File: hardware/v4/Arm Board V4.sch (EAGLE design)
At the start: 43 parts, among them U1 SN74LS241DW, U2 XBEE-1B3, U3 LSM9DS0

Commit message: Nothing much
Nothing much
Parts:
- removed H1, H2, H3, H4: (no value), Lib_TH:H_MNTHOLE_#4
- removed JP4: (no value), SparkFun-Connectors:M04SCREW
- added JP1: (no value), SparkFun-Connectors:M03SCREW
- added S1, S2, S3, S4: STANDOFF_ELECTRICAL, SparkFun-Electromechanical:STANDOFF_ELECTRICAL
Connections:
- net +12V: now also JP1.3; no longer JP4.3
- net +5V: now also U$3.4, U$3.5; no longer JP4.4
- net GND: now also JP1.1, S1.P$1, S2.P$1, S3.P$1, S4.P$1; no longer H1.1, H2.1, H3.1, H4.1, JP4.1
- net VIN: now also JP1.2; no longer JP4.2
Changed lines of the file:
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@@
 <part name="R11" library="SparkFun-Passives" deviceset="RESISTOR" device="1206" value="120 Ohm"/>
 <part name="C12" library="SparkFun-Capacitors" deviceset="CAP" device="1206" value=".1uF"/>
-<part name="H1" library="Lib_TH" deviceset="H_MNTHOLE" device="_#4"/>
-<part name="H2" library="Lib_TH" deviceset="H_MNTHOLE" device="_#4"/>
-<part name="H3" library="Lib_TH" deviceset="H_MNTHOLE" device="_#4"/>
-<part name="H4" library="Lib_TH" deviceset="H_MNTHOLE" device="_#4"/>
-<part name="GND11" library="SparkFun-Aesthetics" deviceset="GND" device=""/>
-<part name="GND12" library="SparkFun-Aesthetics" deviceset="GND" device=""/>
-<part name="GND13" library="SparkFun-Aesthetics" deviceset="GND" device=""/>
-<part name="GND14" library="SparkFun-Aesthetics" deviceset="GND" device=""/>
 <part name="R12" library="SparkFun-Passives" deviceset="RESISTOR" device="1206" value="1k"/>
 <part name="LED1" library="SparkFun-LED" deviceset="LED-RED" device="0603" value="RED"/>
@@
 <part name="LED5" library="SparkFun-LED" deviceset="LED-RED" device="0603" value="RED"/>
 <part name="GND30" library="SparkFun" deviceset="GND" device=""/>
-<part name="JP4" library="SparkFun-Connectors" deviceset="M04" device="SCREW"/>
-<part name="GND3" library="SparkFun-Aesthetics" deviceset="GND" device=""/>
+<part name="S1" library="SparkFun-Electromechanical" deviceset="STANDOFF_ELECTRICAL" device=""/>
+<part name="S2" library="SparkFun-Electromechanical" deviceset="STANDOFF_ELECTRICAL" device=""/>
+<part name="S3" library="SparkFun-Electromechanical" deviceset="STANDOFF_ELECTRICAL" device=""/>
+<part name="S4" library="SparkFun-Electromechanical" deviceset="STANDOFF_ELECTRICAL" device=""/>
+<part name="GND11" library="SparkFun-Aesthetics" deviceset="GND" device=""/>
+<part name="JP1" library="SparkFun-Connectors" deviceset="M03" device="SCREW"/>
+<part name="GND12" library="SparkFun-Aesthetics" deviceset="GND" device=""/>
 </parts>
 <sheets>
@@
 </plain>
 <instances>
-<instance part="H1" gate="G$1" x="25.4" y="38.1"/>
-<instance part="H2" gate="G$1" x="35.56" y="38.1"/>
-<instance part="H3" gate="G$1" x="45.72" y="38.1"/>
-<instance part="H4" gate="G$1" x="55.88" y="38.1"/>
-<instance part="GND11" gate="1" x="25.4" y="30.48"/>
-<instance part="GND12" gate="1" x="35.56" y="30.48"/>
-<instance part="GND13" gate="1" x="45.72" y="30.48"/>
-<instance part="GND14" gate="1" x="55.88" y="30.48"/>
 <instance part="JP7" gate="G$1" x="190.5" y="50.8" rot="R270"/>
 <instance part="JP8" gate="G$1" x="203.2" y="50.8" rot="R270"/>
@@
 <instance part="LED5" gate="G$1" x="15.24" y="-25.4"/>
 <instance part="GND30" gate="1" x="15.24" y="-35.56"/>
-<instance part="JP4" gate="G$1" x="129.54" y="10.16" rot="R270"/>
-<instance part="GND3" gate="1" x="127" y="2.54"/>
+<instance part="S1" gate="G$1" x="25.4" y="58.42" rot="R270"/>
+<instance part="S2" gate="G$1" x="38.1" y="58.42" rot="R270"/>
+<instance part="S3" gate="G$1" x="50.8" y="58.42" rot="R270"/>
+<instance part="S4" gate="G$1" x="63.5" y="58.42" rot="R270"/>
+<instance part="GND11" gate="1" x="43.18" y="45.72"/>
+<instance part="JP1" gate="G$1" x="152.4" y="12.7" rot="R270"/>
+<instance part="GND12" gate="1" x="149.86" y="2.54"/>
 </instances>
 <busses>
@@
 <net name="GND" class="0">
 <segment>
-<pinref part="H1" gate="G$1" pin="1"/>
-<pinref part="GND11" gate="1" pin="GND"/>
-<wire x1="25.4" y1="33.02" x2="25.4" y2="38.1" width="0.1524" layer="91"/>
-</segment>
-<segment>
-<pinref part="H2" gate="G$1" pin="1"/>
-<pinref part="GND12" gate="1" pin="GND"/>
-<wire x1="35.56" y1="33.02" x2="35.56" y2="38.1" width="0.1524" layer="91"/>
-</segment>
-<segment>
-<pinref part="H3" gate="G$1" pin="1"/>
-<pinref part="GND13" gate="1" pin="GND"/>
-<wire x1="45.72" y1="33.02" x2="45.72" y2="38.1" width="0.1524" layer="91"/>
-</segment>
-<segment>
-<pinref part="H4" gate="G$1" pin="1"/>
-<pinref part="GND14" gate="1" pin="GND"/>
-<wire x1="55.88" y1="33.02" x2="55.88" y2="38.1" width="0.1524" layer="91"/>
-</segment>
-<segment>
 <pinref part="JP9" gate="G$1" pin="1"/>
 <pinref part="GND1" gate="1" pin="GND"/>
@@
 </segment>
 <segment>
-<pinref part="JP4" gate="G$1" pin="1"/>
-<pinref part="GND3" gate="1" pin="GND"/>
+<pinref part="S1" gate="G$1" pin="P$1"/>
+<wire x1="25.4" y1="50.8" x2="25.4" y2="48.26" width="0.1524" layer="91"/>
+<pinref part="GND11" gate="1" pin="GND"/>
+<wire x1="25.4" y1="48.26" x2="38.1" y2="48.26" width="0.1524" layer="91"/>
+<pinref part="S2" gate="G$1" pin="P$1"/>
+<wire x1="43.18" y1="48.26" x2="38.1" y2="48.26" width="0.1524" layer="91"/>
+<wire x1="38.1" y1="50.8" x2="38.1" y2="48.26" width="0.1524" layer="91"/>
+<pinref part="S4" gate="G$1" pin="P$1"/>
+<wire x1="63.5" y1="50.8" x2="63.5" y2="48.26" width="0.1524" layer="91"/>
+<wire x1="63.5" y1="48.26" x2="50.8" y2="48.26" width="0.1524" layer="91"/>
+<pinref part="S3" gate="G$1" pin="P$1"/>
+<wire x1="50.8" y1="48.26" x2="43.18" y2="48.26" width="0.1524" layer="91"/>
+<wire x1="50.8" y1="50.8" x2="50.8" y2="48.26" width="0.1524" layer="91"/>
+<junction x="38.1" y="48.26"/>
+<junction x="50.8" y="48.26"/>
+<junction x="43.18" y="48.26"/>
+<junction x="25.4" y="48.26"/>
+<junction x="63.5" y="48.26"/>
+</segment>
+<segment>
+<pinref part="JP1" gate="G$1" pin="1"/>
+<pinref part="GND12" gate="1" pin="GND"/>
 </segment>
 </net>
@@
 </segment>
 <segment>
-<pinref part="JP4" gate="G$1" pin="3"/>
-<wire x1="132.08" y1="5.08" x2="132.08" y2="-10.16" width="0.1524" layer="91"/>
-<label x="132.08" y="-5.08" size="1.778" layer="95" rot="R270"/>
+<wire x1="154.94" y1="5.08" x2="154.94" y2="-5.08" width="0.1524" layer="91"/>
+<pinref part="JP1" gate="G$1" pin="3"/>
 </segment>
 </net>
@@
 <wire x1="190.5" y1="43.18" x2="190.5" y2="38.1" width="0.1524" layer="91"/>
 <label x="190.5" y="38.1" size="1.778" layer="95" rot="R180"/>
-</segment>
-<segment>
-<pinref part="JP4" gate="G$1" pin="4"/>
-<wire x1="134.62" y1="5.08" x2="134.62" y2="-17.78" width="0.1524" layer="91"/>
-<label x="134.62" y="-15.24" size="1.778" layer="95" rot="R270"/>
 </segment>
 </net>
@@
 </segment>
 <segment>
-<pinref part="JP4" gate="G$1" pin="2"/>
-<wire x1="129.54" y1="5.08" x2="129.54" y2="-2.54" width="0.1524" layer="91"/>
-<label x="129.54" y="-2.54" size="1.778" layer="95" rot="R270"/>
+<wire x1="152.4" y1="5.08" x2="152.4" y2="-2.54" width="0.1524" layer="91"/>
+<pinref part="JP1" gate="G$1" pin="2"/>
 </segment>
 </net>
@@
 <pinref part="U$4" gate="G$1" pin="VCC"/>
 </segment>
-</net>
+<segment>
+<pinref part="U$3" gate="G$1" pin="4"/>
+<wire x1="132.08" y1="15.24" x2="129.54" y2="15.24" width="0.1524" layer="91"/>
+<wire x1="129.54" y1="15.24" x2="129.54" y2="12.7" width="0.1524" layer="91"/>
+<pinref part="U$3" gate="G$1" pin="5"/>
+<wire x1="129.54" y1="12.7" x2="132.08" y2="12.7" width="0.1524" layer="91"/>
+</segment>
+</net>

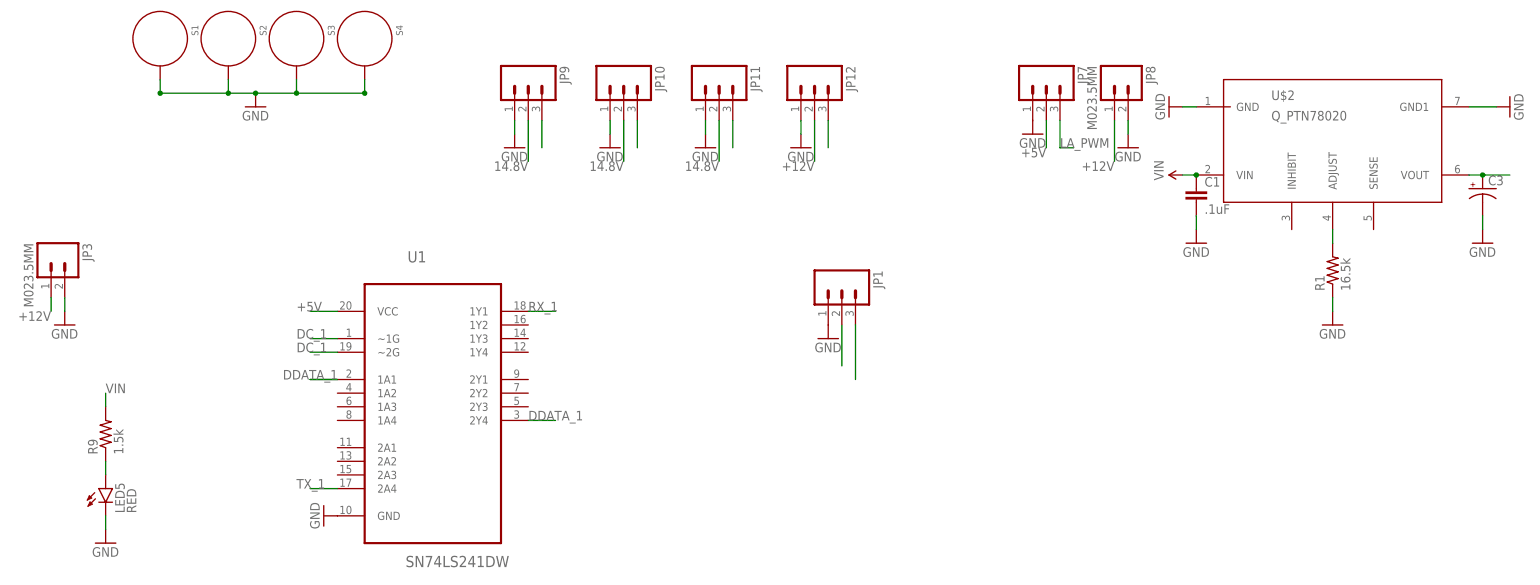
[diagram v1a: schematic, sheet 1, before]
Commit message: Implemented PoRN and Switched Power Connectors
Implemented PoRN(PoRC) and switched to 3.5mm screw terminals
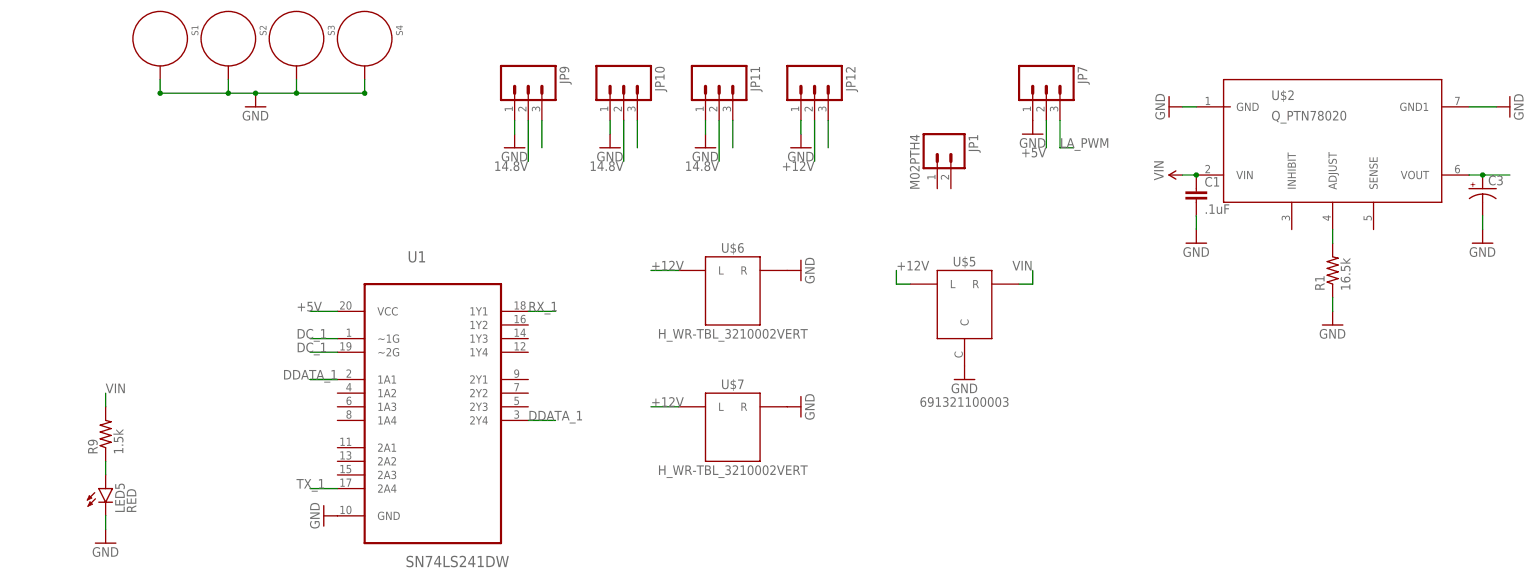
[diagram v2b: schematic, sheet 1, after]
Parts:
- removed JP3, JP8: M023.5MM, SparkFun-Connectors:M023.5MM
- added U$5: 691321100003, MRDT-2015-PowerBoard:691321100003
- added U$6, U$7: H_WR-TBL_3210002VERT, MRDT-2015-PowerBoard:H_WR-TBL_3210002VERT
- JP1: value (none) -> M02PTH4; device SparkFun-Connectors:M03SCREW -> SparkFun-Connectors:M02PTH4
- JP10, JP11, JP12, JP7, JP9: device SparkFun-Connectors:M03POLAR -> SparkFun-Connectors:M03PTH
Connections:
- net +12V: now also U$5.L, U$6.L, U$7.L; no longer JP1.3, JP3.1, JP8.1
- net GND: now also U$5.C, U$6.R, U$7.R; no longer JP1.1, JP3.2, JP8.2
- net VIN: now also U$5.R; no longer JP1.2
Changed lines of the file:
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@@
 <part name="R14" library="SparkFun-Passives" deviceset="RESISTOR" device="1206" value="1k"/>
 <part name="U2" library="SparkFun" deviceset="XBEE-1" device="B3"/>
-<part name="JP7" library="SparkFun-Connectors" deviceset="M03" device="POLAR"/>
-<part name="JP8" library="SparkFun-Connectors" deviceset="M02" device="3.5MM" value="M023.5MM"/>
-<part name="JP9" library="SparkFun-Connectors" deviceset="M03" device="POLAR"/>
-<part name="JP10" library="SparkFun-Connectors" deviceset="M03" device="POLAR"/>
-<part name="JP11" library="SparkFun-Connectors" deviceset="M03" device="POLAR"/>
-<part name="JP12" library="SparkFun-Connectors" deviceset="M03" device="POLAR"/>
+<part name="JP7" library="SparkFun-Connectors" deviceset="M03" device="PTH"/>
+<part name="JP9" library="SparkFun-Connectors" deviceset="M03" device="PTH"/>
+<part name="JP10" library="SparkFun-Connectors" deviceset="M03" device="PTH"/>
+<part name="JP11" library="SparkFun-Connectors" deviceset="M03" device="PTH"/>
+<part name="JP12" library="SparkFun-Connectors" deviceset="M03" device="PTH"/>
 <part name="GND1" library="SparkFun-Aesthetics" deviceset="GND" device=""/>
 <part name="GND2" library="SparkFun-Aesthetics" deviceset="GND" device=""/>
 <part name="GND4" library="SparkFun-Aesthetics" deviceset="GND" device=""/>
 <part name="GND5" library="SparkFun-Aesthetics" deviceset="GND" device=""/>
-<part name="GND9" library="SparkFun-Aesthetics" deviceset="GND" device=""/>
 <part name="GND10" library="SparkFun-Aesthetics" deviceset="GND" device=""/>
 <part name="U$2" library="MRDT-2014-All" deviceset="Q_PTN78020" device=""/>
@@
 <part name="C3" library="SparkFun-Passives" deviceset="CAP_POL" device="C"/>
 <part name="U$4" library="MAX3077" deviceset="MAX3077" device=""/>
-<part name="JP3" library="SparkFun-Connectors" deviceset="M02" device="3.5MM" value="M023.5MM"/>
-<part name="GND6" library="SparkFun-Aesthetics" deviceset="GND" device=""/>
 <part name="U3" library="SparkFun-DigitalIC" deviceset="LSM9DS0" device=""/>
 <part name="C5" library="SparkFun-Capacitors" deviceset="CAP" device="1206" value=".22uF"/>
@@
 <part name="S4" library="SparkFun-Electromechanical" deviceset="STANDOFF_ELECTRICAL" device=""/>
 <part name="GND11" library="SparkFun-Aesthetics" deviceset="GND" device=""/>
-<part name="JP1" library="SparkFun-Connectors" deviceset="M03" device="SCREW"/>
-<part name="GND12" library="SparkFun-Aesthetics" deviceset="GND" device=""/>
+<part name="U$5" library="MRDT-2015-PowerBoard" deviceset="691321100003" device=""/>
+<part name="GND3" library="SparkFun-Aesthetics" deviceset="GND" device=""/>
+<part name="U$6" library="MRDT-2015-PowerBoard" deviceset="H_WR-TBL_32*1*0002" device="VERT"/>
+<part name="U$7" library="MRDT-2015-PowerBoard" deviceset="H_WR-TBL_32*1*0002" device="VERT"/>
+<part name="GND6" library="SparkFun-Aesthetics" deviceset="GND" device=""/>
+<part name="GND9" library="SparkFun-Aesthetics" deviceset="GND" device=""/>
+<part name="JP1" library="SparkFun-Connectors" deviceset="M02" device="PTH4"/>
 </parts>
 <sheets>
@@
 <instances>
 <instance part="JP7" gate="G$1" x="190.5" y="50.8" rot="R270"/>
-<instance part="JP8" gate="G$1" x="203.2" y="50.8" rot="R270"/>
 <instance part="JP9" gate="G$1" x="93.98" y="50.8" rot="R270"/>
 <instance part="JP10" gate="G$1" x="111.76" y="50.8" rot="R270"/>
@@
 <instance part="GND4" gate="1" x="127" y="38.1"/>
 <instance part="GND5" gate="1" x="144.78" y="38.1"/>
-<instance part="GND9" gate="1" x="205.74" y="38.1"/>
 <instance part="GND10" gate="1" x="187.96" y="40.64"/>
 <instance part="U$2" gate="G$1" x="223.52" y="45.72"/>
@@
 <instance part="GND21" gate="1" x="271.78" y="20.32"/>
 <instance part="C3" gate="G$1" x="271.78" y="30.48"/>
-<instance part="JP3" gate="G$1" x="5.08" y="17.78" rot="R270"/>
-<instance part="GND6" gate="1" x="7.62" y="5.08"/>
 <instance part="R9" gate="G$1" x="15.24" y="-15.24" rot="R90"/>
 <instance part="LED5" gate="G$1" x="15.24" y="-25.4"/>
@@
 <instance part="S4" gate="G$1" x="63.5" y="58.42" rot="R270"/>
 <instance part="GND11" gate="1" x="43.18" y="45.72"/>
-<instance part="JP1" gate="G$1" x="152.4" y="12.7" rot="R270"/>
-<instance part="GND12" gate="1" x="149.86" y="2.54"/>
+<instance part="U$5" gate="G$1" x="175.26" y="10.16"/>
+<instance part="GND3" gate="1" x="175.26" y="-5.08"/>
+<instance part="U$6" gate="G$1" x="132.08" y="12.7"/>
+<instance part="U$7" gate="G$1" x="132.08" y="-12.7"/>
+<instance part="GND6" gate="1" x="144.78" y="15.24" rot="R90"/>
+<instance part="GND9" gate="1" x="144.78" y="-10.16" rot="R90"/>
+<instance part="JP1" gate="G$1" x="170.18" y="38.1" rot="R270"/>
 </instances>
 <busses>
@@
 </segment>
 <segment>
-<pinref part="JP8" gate="G$1" pin="2"/>
-<pinref part="GND9" gate="1" pin="GND"/>
-<wire x1="205.74" y1="43.18" x2="205.74" y2="40.64" width="0.1524" layer="91"/>
-</segment>
-<segment>
 <pinref part="JP7" gate="G$1" pin="1"/>
 <pinref part="GND10" gate="1" pin="GND"/>
@@
 <wire x1="271.78" y1="22.86" x2="271.78" y2="25.4" width="0.1524" layer="91"/>
 <pinref part="C3" gate="G$1" pin="-"/>
-</segment>
-<segment>
-<pinref part="JP3" gate="G$1" pin="2"/>
-<pinref part="GND6" gate="1" pin="GND"/>
-<wire x1="7.62" y1="7.62" x2="7.62" y2="10.16" width="0.1524" layer="91"/>
 </segment>
 <segment>
@@
 </segment>
 <segment>
-<pinref part="JP1" gate="G$1" pin="1"/>
-<pinref part="GND12" gate="1" pin="GND"/>
+<pinref part="U$5" gate="G$1" pin="C"/>
+<pinref part="GND3" gate="1" pin="GND"/>
+</segment>
+<segment>
+<pinref part="U$6" gate="G$1" pin="R"/>
+<pinref part="GND6" gate="1" pin="GND"/>
+</segment>
+<segment>
+<pinref part="U$7" gate="G$1" pin="R"/>
+<pinref part="GND9" gate="1" pin="GND"/>
 </segment>
 </net>
 <net name="+12V" class="0">
-<segment>
-<wire x1="203.2" y1="43.18" x2="203.2" y2="35.56" width="0.1524" layer="91"/>
-<label x="203.2" y="35.56" size="1.778" layer="95" rot="R180"/>
-<pinref part="JP8" gate="G$1" pin="1"/>
-</segment>
 <segment>
 <wire x1="147.32" y1="43.18" x2="147.32" y2="35.56" width="0.1524" layer="91"/>
@@
 </segment>
 <segment>
-<pinref part="JP3" gate="G$1" pin="1"/>
-<wire x1="5.08" y1="10.16" x2="5.08" y2="7.62" width="0.1524" layer="91"/>
-<label x="5.08" y="7.62" size="1.778" layer="95" rot="R180"/>
-</segment>
-<segment>
-<wire x1="154.94" y1="5.08" x2="154.94" y2="-5.08" width="0.1524" layer="91"/>
-<pinref part="JP1" gate="G$1" pin="3"/>
+<pinref part="U$5" gate="G$1" pin="L"/>
+<wire x1="165.1" y1="12.7" x2="162.56" y2="12.7" width="0.1524" layer="91"/>
+<wire x1="162.56" y1="12.7" x2="162.56" y2="15.24" width="0.1524" layer="91"/>
+<label x="162.56" y="15.24" size="1.778" layer="95"/>
+</segment>
+<segment>
+<pinref part="U$6" gate="G$1" pin="L"/>
+<wire x1="121.92" y1="15.24" x2="116.84" y2="15.24" width="0.1524" layer="91"/>
+<label x="116.84" y="15.24" size="1.778" layer="95"/>
+</segment>
+<segment>
+<pinref part="U$7" gate="G$1" pin="L"/>
+<wire x1="121.92" y1="-10.16" x2="116.84" y2="-10.16" width="0.1524" layer="91"/>
+<label x="116.84" y="-10.16" size="1.778" layer="95"/>
 </segment>
 </net>
@@
 </segment>
 <segment>
-<wire x1="152.4" y1="5.08" x2="152.4" y2="-2.54" width="0.1524" layer="91"/>
-<pinref part="JP1" gate="G$1" pin="2"/>
-</segment>
-</net>
+<pinref part="U$5" gate="G$1" pin="R"/>
+<wire x1="185.42" y1="12.7" x2="187.96" y2="12.7" width="0.1524" layer="91"/>
+<wire x1="187.96" y1="12.7" x2="187.96" y2="15.24" width="0.1524" layer="91"/>
+<label x="187.96" y="15.24" size="1.778" layer="95" rot="MR0"/>
+</segment>
+</net>
